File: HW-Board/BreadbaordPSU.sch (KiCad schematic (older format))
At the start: 30 parts, among them J1 vin, J2 Outputs, Q1 Si4435, U1 MAX6241

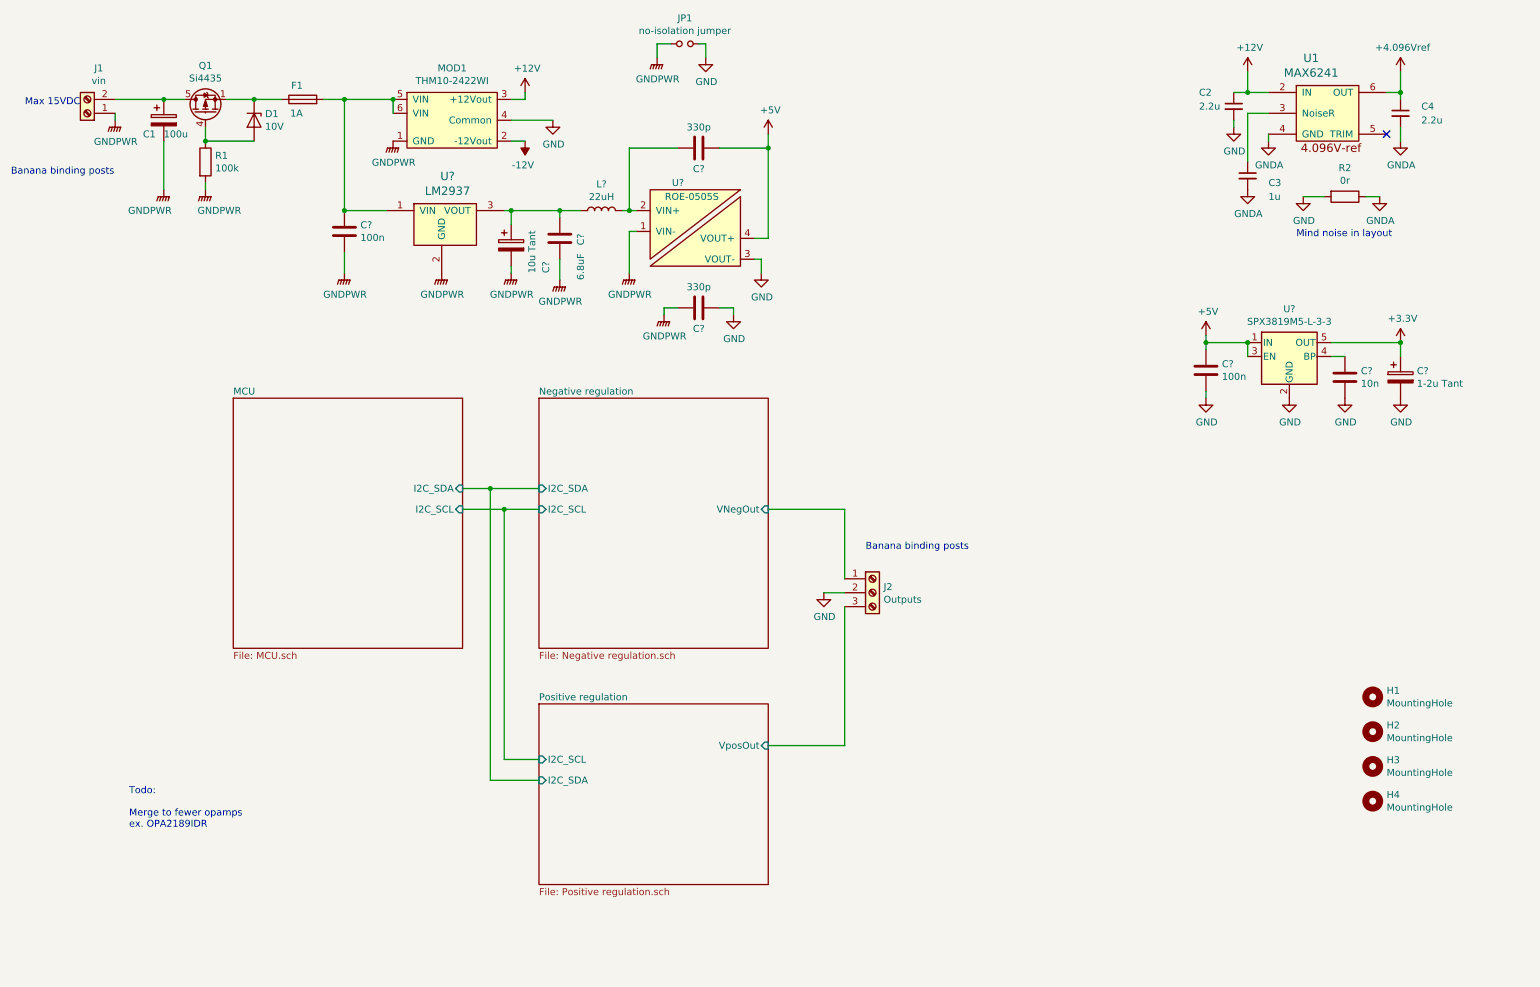
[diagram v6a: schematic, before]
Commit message: Boost converter added
Go go abvoe Vgs-th at maximum output
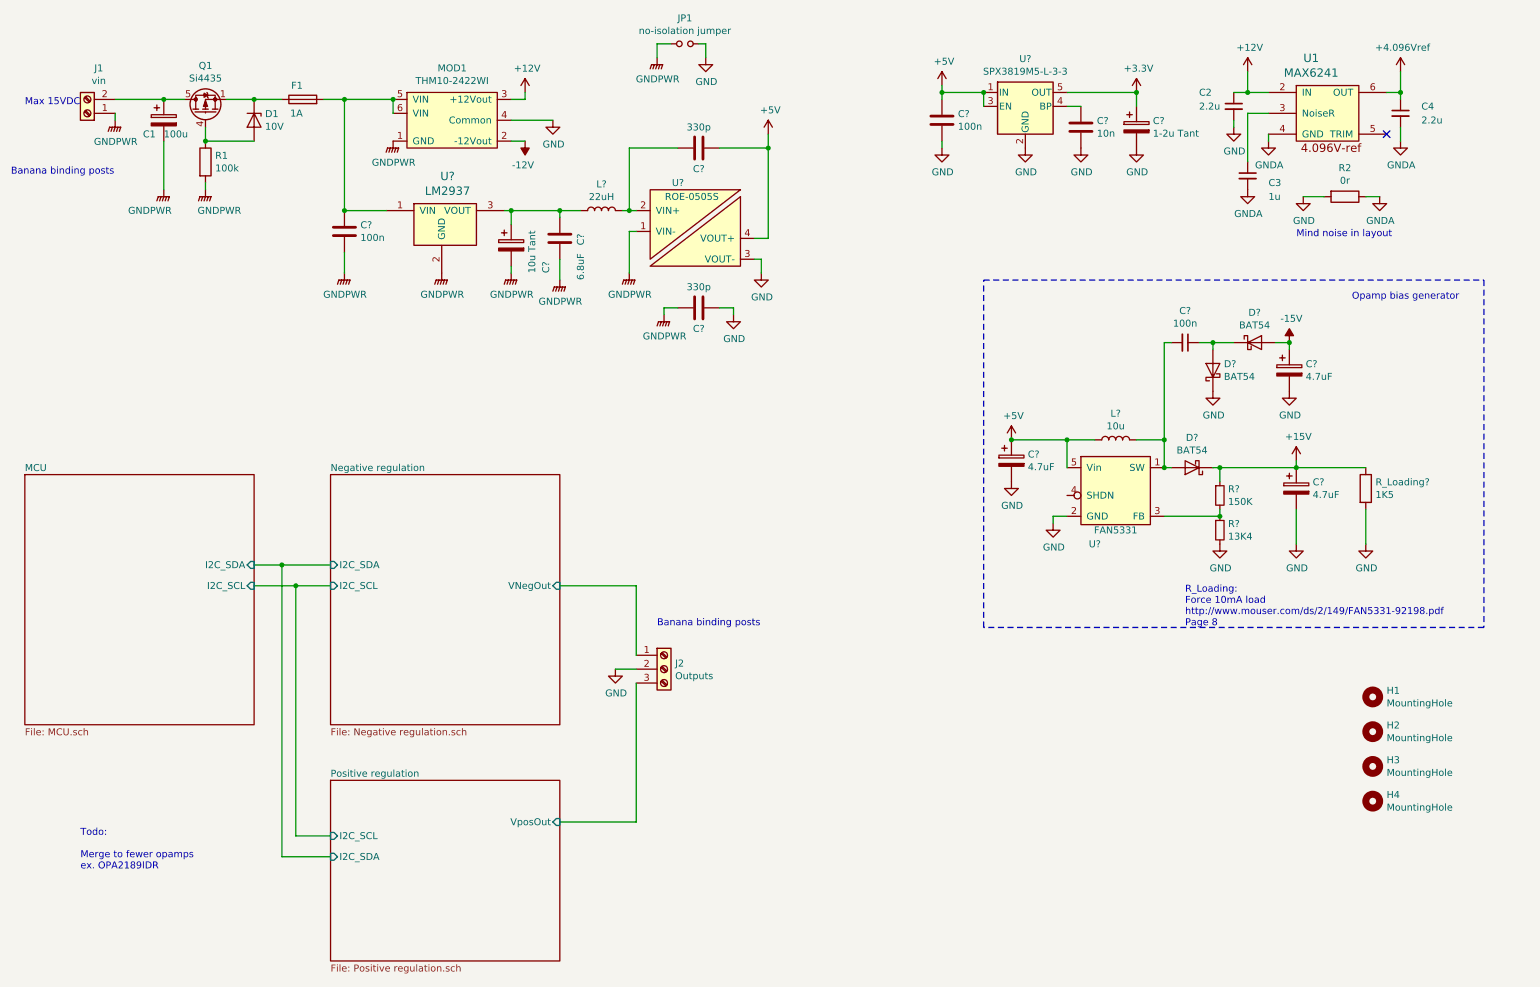
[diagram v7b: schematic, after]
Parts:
- added C? (x3): 4.7uF, symbol Device:CP
- added C?: 100n, symbol Device:C_Small
- added D? (x3): BAT54, symbol Device:D_Schottky
- added L?: 10u, symbol Device:L
- added R?: 150K, symbol Device:R_Small
- added R?: 13K4, symbol Device:R_Small
- added R_Loading?: 1K5, symbol Device:R
- added U?: FAN5331, Package_TO_SOT_SMD:SOT-23-5_HandSoldering, symbol Peters:FAN5331
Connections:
- net +5V: now also C?.1, L?.1, U?.5 (Vin)
- net GND: now also C?.2, C?.2, C?.2, D?.1 (K), R?.2, R_Loading?.2, U?.2 (GND)
- new net: C?.2, D?.2 (A), L?.2, U?.1 (SW)
- new net: R?.1, R?.2, U?.3 (FB)
- new net: C?.1, D?.1 (K), D?.2 (A)
- new net +15V: C?.1, D?.1 (K), R?.1, R_Loading?.1
- new net -15V: C?.1, D?.2 (A)
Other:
- note added: "Opamp bias generator"
- note added: "R_Loading:\nForce 10mA load\nhttp://www.mouser.com/ds/2/149/FAN5331-92198.pdf\nPage 8"
- moved on the sheet: C?, J2, U?

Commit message: Negative regulation done
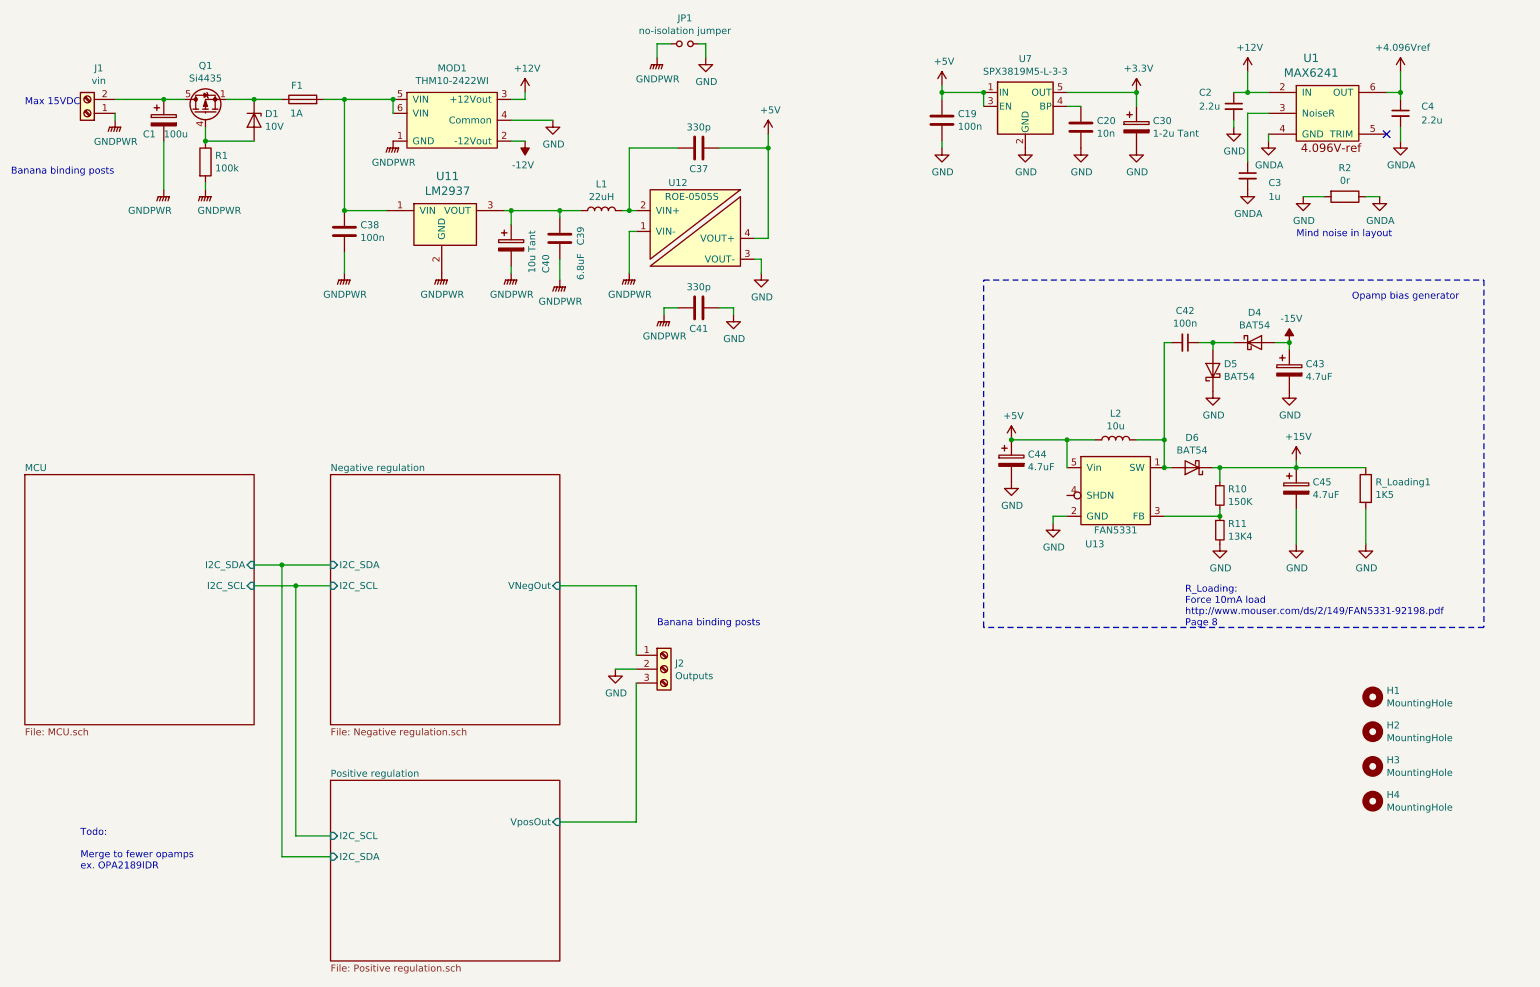
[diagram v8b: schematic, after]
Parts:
- C19, C20, C37, C38, C41, C42: renamed from C?; footprint (none) -> Capacitor_SMD:C_0805_2012Metric_Pad1.15x1.40mm_HandSolder
- C3, C4: footprint (none) -> Capacitor_SMD:C_0805_2012Metric_Pad1.15x1.40mm_HandSolder
- R1: footprint (none) -> Resistor_SMD:R_0805_2012Metric_Pad1.15x1.40mm_HandSolder
- R10, R11: renamed from R?; footprint (none) -> Resistor_SMD:R_0805_2012Metric_Pad1.15x1.40mm_HandSolder
- R2: footprint (none) -> Resistor_SMD:R_1210_3225Metric_Pad1.42x2.65mm_HandSolder
- R_Loading1: renamed from R_Loading?; footprint (none) -> Resistor_SMD:R_0805_2012Metric_Pad1.15x1.40mm_HandSolder
- gave numbers to parts that had none: 15
